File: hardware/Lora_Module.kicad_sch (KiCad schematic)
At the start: 0 parts

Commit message: Main modules added + Com lines
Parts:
- added U7: RFM95W-868S2, RF_Module:HOPERF_RFM9XW_SMD, symbol RF_Module:RFM95W-868S2
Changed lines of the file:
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@@
 	(generator_version "9.0")
 	(paper "A4")
+	(global_label "SPI_SELECT"
+		(shape input)
+		(at 39.37 59.69 180)
+		(fields_autoplaced yes)
+		(effects
+			(font
+				(size 1.27 1.27)
+			)
+			(justify right)
+		)
+		(property "Intersheetrefs" "${INTERSHEET_REFS}"
+			(at 25.5597 59.69 0)
+			(effects
+				(font
+					(size 1.27 1.27)
+				)
+				(justify right)
+				(hide yes)
+			)
+		)
+	)
+	(global_label "SPI_MOSI"
+		(shape input)
+		(at 39.37 62.23 180)
+		(fields_autoplaced yes)
+		(effects
+			(font
+				(size 1.27 1.27)
+			)
+			(justify right)
+		)
+		(property "Intersheetrefs" "${INTERSHEET_REFS}"
+			(at 27.7367 62.23 0)
+			(effects
+				(font
+					(size 1.27 1.27)
+				)
+				(justify right)
+				(hide yes)
+			)
+		)
+	)
+	(global_label "3.3V"
+		(shape input)
+		(at 35.56 38.1 180)
+		(fields_autoplaced yes)
+		(effects
+			(font
+				(size 1.27 1.27)
+			)
+			(justify right)
+		)
+		(property "Intersheetrefs" "${INTERSHEET_REFS}"
+			(at 28.4624 38.1 0)
+			(effects
+				(font
+					(size 1.27 1.27)
+				)
+				(justify right)
+				(hide yes)
+			)
+		)
+	)
+	(global_label "SPI_MISO"
+		(shape output)
+		(at 39.37 64.77 180)
+		(fields_autoplaced yes)
+		(effects
+			(font
+				(size 1.27 1.27)
+			)
+			(justify right)
+		)
+		(property "Intersheetrefs" "${INTERSHEET_REFS}"
+			(at 27.7367 64.77 0)
+			(effects
+				(font
+					(size 1.27 1.27)
+				)
+				(justify right)
+				(hide yes)
+			)
+		)
+	)
+	(global_label "SPI_CLK"
+		(shape input)
+		(at 39.37 67.31 180)
+		(fields_autoplaced yes)
+		(effects
+			(font
+				(size 1.27 1.27)
+			)
+			(justify right)
+		)
+		(property "Intersheetrefs" "${INTERSHEET_REFS}"
+			(at 28.7648 67.31 0)
+			(effects
+				(font
+					(size 1.27 1.27)
+				)
+				(justify right)
+				(hide yes)
+			)
+		)
+	)
+	(symbol
+		(lib_id "RF_Module:RFM95W-868S2")
+		(at 109.22 72.39 0)
+		(unit 1)
+		(exclude_from_sim no)
+		(in_bom yes)
+		(on_board yes)
+		(dnp no)
+		(fields_autoplaced yes)
+		(property "Reference" "U7"
+			(at 111.3633 57.15 0)
+			(effects
+				(font
+					(size 1.27 1.27)
+				)
+				(justify left)
+			)
+		)
+		(property "Value" "RFM95W-868S2"
+			(at 111.3633 59.69 0)
+			(effects
+				(font
+					(size 1.27 1.27)
+				)
+				(justify left)
+			)
+		)
+		(property "Footprint" "RF_Module:HOPERF_RFM9XW_SMD"
+			(at 25.4 30.48 0)
+			(effects
+				(font
+					(size 1.27 1.27)
+				)
+				(hide yes)
+			)
+		)
+		(property "Datasheet" "https://www.hoperf.com/data/upload/portal/20181127/5bfcbea20e9ef.pdf"
+			(at 25.4 30.48 0)
+			(effects
+				(font
+					(size 1.27 1.27)
+				)
+				(hide yes)
+			)
+		)
+		(property "Description" "Low power long range transceiver module, SPI and parallel interface, 868 MHz, spreading factor 6 to12, bandwidth 7.8 to 500kHz, -111 to -148 dBm, SMD-16, DIP-16"
+			(at 109.22 72.39 0)
+			(effects
+				(font
+					(size 1.27 1.27)
+				)
+				(hide yes)
+			)
+		)
+		(pin "3"
+		)
+		(pin "4"
+		)
+		(pin "2"
+		)
+		(pin "5"
+		)
+		(pin "6"
+		)
+		(pin "1"
+		)
+		(pin "13"
+		)
+		(pin "8"
+		)
+		(pin "10"
+		)
+		(pin "9"
+		)
+		(pin "11"
+		)
+		(pin "7"
+		)
+		(pin "14"
+		)
+		(pin "12"
+		)
+		(pin "16"
+		)
+		(pin "15"
+		)
+		(instances
+			(project ""
+				(path "/5b969f6e-a36e-432b-8f00-b2d6a515a877/9db73a32-37a4-4249-8656-c1ba9b3afe01"
+					(reference "U7")
+					(unit 1)
+				)
+			)
+		)
+	)
 )

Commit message: GPS schematic + datasheet
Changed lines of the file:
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@@
 	(global_label "SPI_SELECT"
 		(shape input)
-		(at 39.37 59.69 180)
+		(at 66.04 64.77 180)
 		(fields_autoplaced yes)
 		(effects
@@
 		)
 		(property "Intersheetrefs" "${INTERSHEET_REFS}"
-			(at 25.5597 59.69 0)
+			(at 52.2297 64.77 0)
 			(effects
 				(font
@@
 	(global_label "SPI_MOSI"
 		(shape input)
-		(at 39.37 62.23 180)
+		(at 66.04 67.31 180)
 		(fields_autoplaced yes)
 		(effects
@@
 		)
 		(property "Intersheetrefs" "${INTERSHEET_REFS}"
-			(at 27.7367 62.23 0)
+			(at 54.4067 67.31 0)
 			(effects
 				(font
@@
 	(global_label "3.3V"
 		(shape input)
-		(at 35.56 38.1 180)
+		(at 72.39 53.34 180)
 		(fields_autoplaced yes)
 		(effects
@@
 		)
 		(property "Intersheetrefs" "${INTERSHEET_REFS}"
-			(at 28.4624 38.1 0)
+			(at 65.2924 53.34 0)
 			(effects
 				(font
@@
 	(global_label "SPI_MISO"
 		(shape output)
-		(at 39.37 64.77 180)
+		(at 66.04 69.85 180)
 		(fields_autoplaced yes)
 		(effects
@@
 		)
 		(property "Intersheetrefs" "${INTERSHEET_REFS}"
-			(at 27.7367 64.77 0)
+			(at 54.4067 69.85 0)
 			(effects
 				(font
@@
 	(global_label "SPI_CLK"
 		(shape input)
-		(at 39.37 67.31 180)
+		(at 66.04 72.39 180)
 		(fields_autoplaced yes)
 		(effects
@@
 		)
 		(property "Intersheetrefs" "${INTERSHEET_REFS}"
-			(at 28.7648 67.31 0)
+			(at 55.4348 72.39 0)
 			(effects
 				(font

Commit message: Found all diodes & transistors footprint & JLCPCB
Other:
- company: (none) -> ECAM Brussels Engineering School
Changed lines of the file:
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@@
 	(generator_version "9.0")
 	(paper "A4")
+	(title_block
+		(rev "0.1")
+		(company "ECAM Brussels Engineering School")
+	)
 	(global_label "SPI_SELECT"
 		(shape input)

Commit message: Module Lora
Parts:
- added C10: 100nF, Capacitor_SMD:C_0201_0603Metric, symbol Device:C
- added C11, C12: C, Capacitor_SMD:C_0805_2012Metric_Pad1.18x1.45mm_HandSolder, symbol Device:C
- added J2: 85201239, SMA-85201239:HUBER_SUHNER_85201239, symbol SMA-85201239:85201239
- added R8: 0, Resistor_SMD:R_0805_2012Metric_Pad1.20x1.40mm_HandSolder, symbol Device:R
- added TP_DIO0, TP_RESET, TP_VCC_Lora: TestPoint, TestPoint:TestPoint_Pad_D2.0mm, symbol Connector:TestPoint
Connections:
- net 3.3V: now also U7.13 (3.3V), C10.2, TP_VCC_Lora.1
- net SPI_CLK: now also U7.4 (SCK)
- net SPI_MISO: now also U7.2 (MISO)
- net SPI_MOSI: now also U7.3 (MOSI)
- net SPI_SELECT: now also U7.5 (NSS)
- net GND: now reaches U7.1 (GND)
- net GND: now also U7.10 (GND), U7.8 (GND), C10.1, C11.2, C12.2, J2.G1, J2.G2, J2.G3, J2.G4
- net DIO0: now reaches U7.14 (DIO0)
- net DIO0: now also TP_DIO0.1
- net RESET: now reaches U7.6 (RESET)
- net RESET: now also TP_RESET.1
- net at U7.9 (ANT): now also C12.1, R8.2
- new net: C11.1, J2.1, R8.1

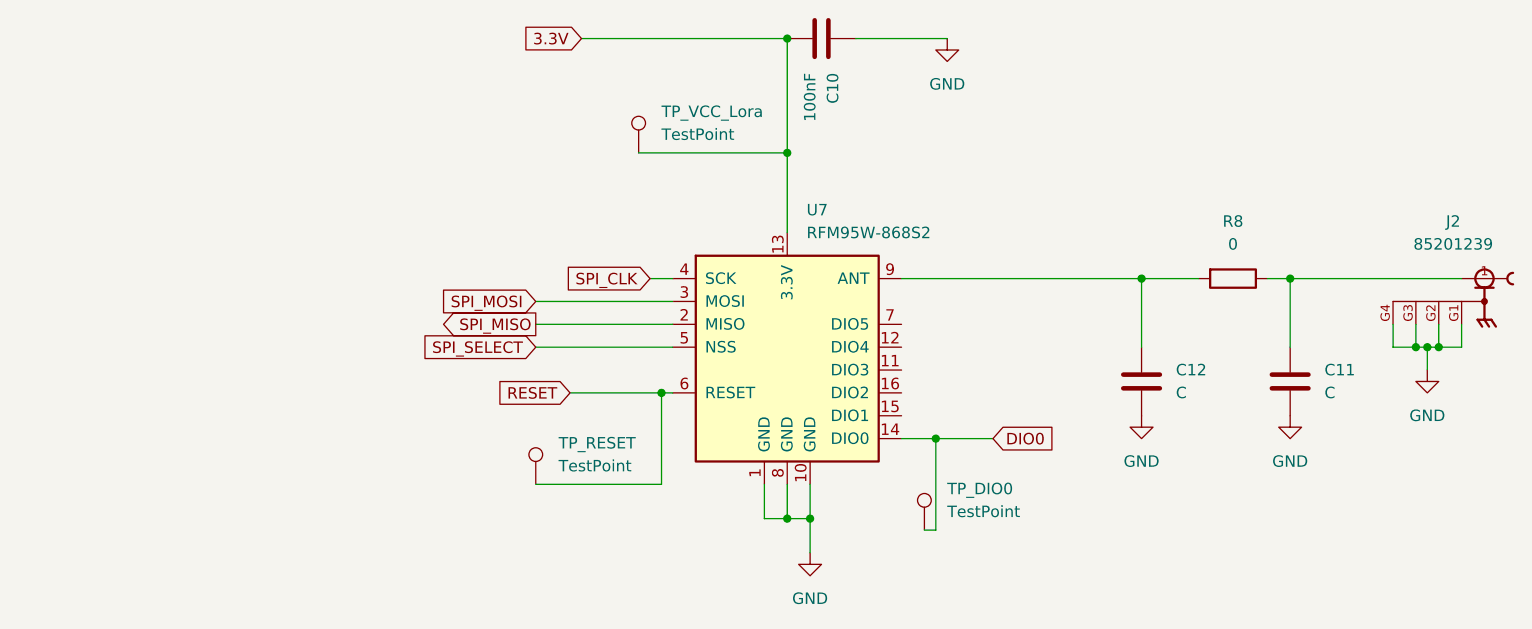
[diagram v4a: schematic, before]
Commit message: Update ESP32 pins
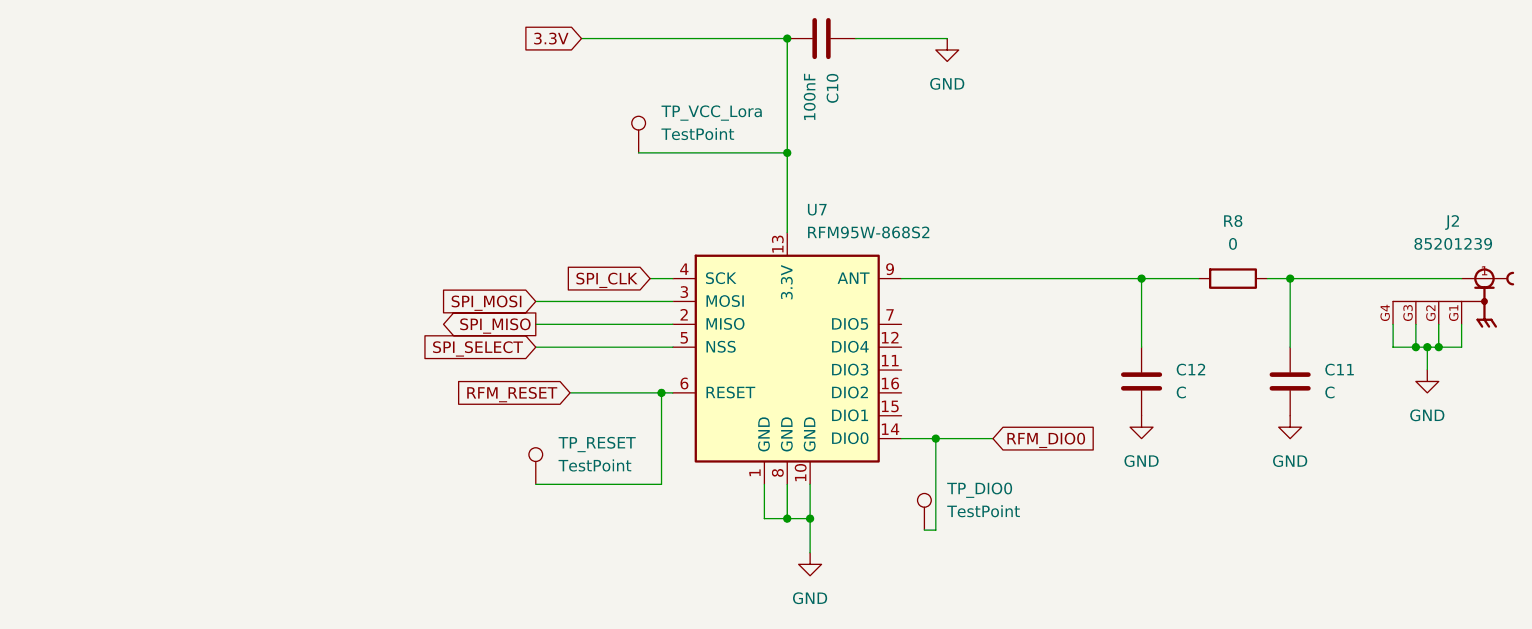
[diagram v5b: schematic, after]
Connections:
- net DIO0 renamed RFM_DIO0
- net RESET renamed RFM_RESET
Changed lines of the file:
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@@
 		)
 	)
-	(global_label "RESET"
+	(global_label "RFM_RESET"
 		(shape input)
 		(at 85.09 77.47 180)
@@
 		)
 		(property "Intersheetrefs" "${INTERSHEET_REFS}"
-			(at 76.3597 77.47 0)
+			(at 71.5821 77.47 0)
 			(effects
 				(font
@@
 		)
 	)
-	(global_label "DIO0"
+	(global_label "RFM_DIO0"
 		(shape input)
 		(at 132.08 82.55 0)
@@
 		)
 		(property "Intersheetrefs" "${INTERSHEET_REFS}"
-			(at 139.48 82.55 0)
+			(at 144.2576 82.55 0)
 			(effects
 				(font

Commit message: First draft
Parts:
- renumbered C10 to C4, C12 to C5, C11 to C6, J2 to J5, R8 to R9, TP_DIO0 to TP_DIO1, TP_RESET to TP_RESET1, TP_VCC_Lora to TP_VCC_Lora1, U7 to U3
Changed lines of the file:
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@@
 		(dnp no)
 		(fields_autoplaced yes)
-		(property "Reference" "TP_DIO0"
+		(property "Reference" "TP_DIO1"
 			(at 127 88.1379 0)
 			(effects
@@
 			(project ""
 				(path "/5b969f6e-a36e-432b-8f00-b2d6a515a877/9db73a32-37a4-4249-8656-c1ba9b3afe01"
-					(reference "TP_DIO0")
+					(reference "TP_DIO1")
 					(unit 1)
 				)
@@
 		(on_board yes)
 		(dnp no)
-		(property "Reference" "J2"
+		(property "Reference" "J5"
 			(at 183.2229 58.42 0)
 			(effects
@@
 			(project ""
 				(path "/5b969f6e-a36e-432b-8f00-b2d6a515a877/9db73a32-37a4-4249-8656-c1ba9b3afe01"
-					(reference "J2")
+					(reference "J5")
 					(unit 1)
 				)
@@
 		(dnp no)
 		(fields_autoplaced yes)
-		(property "Reference" "C12"
+		(property "Reference" "C5"
 			(at 152.4 74.9299 0)
 			(effects
@@
 			(project ""
 				(path "/5b969f6e-a36e-432b-8f00-b2d6a515a877/9db73a32-37a4-4249-8656-c1ba9b3afe01"
-					(reference "C12")
+					(reference "C5")
 					(unit 1)
 				)
@@
 		(dnp no)
 		(fields_autoplaced yes)
-		(property "Reference" "R8"
+		(property "Reference" "R9"
 			(at 158.75 58.42 90)
 			(effects
@@
 			(project ""
 				(path "/5b969f6e-a36e-432b-8f00-b2d6a515a877/9db73a32-37a4-4249-8656-c1ba9b3afe01"
-					(reference "R8")
+					(reference "R9")
 					(unit 1)
 				)
@@
 		(dnp no)
 		(fields_autoplaced yes)
-		(property "Reference" "TP_RESET"
+		(property "Reference" "TP_RESET1"
 			(at 83.82 83.0579 0)
 			(effects
@@
 			(project ""
 				(path "/5b969f6e-a36e-432b-8f00-b2d6a515a877/9db73a32-37a4-4249-8656-c1ba9b3afe01"
-					(reference "TP_RESET")
+					(reference "TP_RESET1")
 					(unit 1)
 				)
@@
 		(dnp no)
 		(fields_autoplaced yes)
-		(property "Reference" "C11"
+		(property "Reference" "C6"
 			(at 168.91 74.9299 0)
 			(effects
@@
 			(project ""
 				(path "/5b969f6e-a36e-432b-8f00-b2d6a515a877/9db73a32-37a4-4249-8656-c1ba9b3afe01"
-					(reference "C11")
+					(reference "C6")
 					(unit 1)
 				)
@@
 		(dnp no)
 		(fields_autoplaced yes)
-		(property "Reference" "U7"
+		(property "Reference" "U3"
 			(at 111.3633 57.15 0)
 			(effects
@@
 			(project ""
 				(path "/5b969f6e-a36e-432b-8f00-b2d6a515a877/9db73a32-37a4-4249-8656-c1ba9b3afe01"
-					(reference "U7")
+					(reference "U3")
 					(unit 1)
 				)
@@
 		(dnp no)
 		(fields_autoplaced yes)
-		(property "Reference" "#PWR06"
+		(property "Reference" "#PWR012"
 			(at 127 44.45 0)
 			(effects
@@
 			(project ""
 				(path "/5b969f6e-a36e-432b-8f00-b2d6a515a877/9db73a32-37a4-4249-8656-c1ba9b3afe01"
-					(reference "#PWR06")
+					(reference "#PWR012")
 					(unit 1)
 				)
@@
 		(dnp no)
 		(fields_autoplaced yes)
-		(property "Reference" "TP_VCC_Lora"
+		(property "Reference" "TP_VCC_Lora1"
 			(at 95.25 46.2279 0)
 			(effects
@@
 			(project ""
 				(path "/5b969f6e-a36e-432b-8f00-b2d6a515a877/9db73a32-37a4-4249-8656-c1ba9b3afe01"
-					(reference "TP_VCC_Lora")
+					(reference "TP_VCC_Lora1")
 					(unit 1)
 				)
@@
 		(dnp no)
 		(fields_autoplaced yes)
-		(property "Reference" "#PWR017"
+		(property "Reference" "#PWR014"
 			(at 165.1 86.36 0)
 			(effects
@@
 			(project ""
 				(path "/5b969f6e-a36e-432b-8f00-b2d6a515a877/9db73a32-37a4-4249-8656-c1ba9b3afe01"
-					(reference "#PWR017")
+					(reference "#PWR014")
 					(unit 1)
 				)
@@
 		(dnp no)
 		(fields_autoplaced yes)
-		(property "Reference" "#PWR018"
+		(property "Reference" "#PWR013"
 			(at 148.59 86.36 0)
 			(effects
@@
 			(project ""
 				(path "/5b969f6e-a36e-432b-8f00-b2d6a515a877/9db73a32-37a4-4249-8656-c1ba9b3afe01"
-					(reference "#PWR018")
+					(reference "#PWR013")
 					(unit 1)
 				)
@@
 		(on_board yes)
 		(dnp no)
-		(property "Reference" "C10"
+		(property "Reference" "C4"
 			(at 114.3001 41.91 0)
 			(effects
@@
 			(project "GOG"
 				(path "/5b969f6e-a36e-432b-8f00-b2d6a515a877/9db73a32-37a4-4249-8656-c1ba9b3afe01"
-					(reference "C10")
+					(reference "C4")
 					(unit 1)
 				)
@@
 		(dnp no)
 		(fields_autoplaced yes)
-		(property "Reference" "#PWR07"
+		(property "Reference" "#PWR011"
 			(at 111.76 101.6 0)
 			(effects
@@
 			(project ""
 				(path "/5b969f6e-a36e-432b-8f00-b2d6a515a877/9db73a32-37a4-4249-8656-c1ba9b3afe01"
-					(reference "#PWR07")
+					(reference "#PWR011")
 					(unit 1)
 				)
@@
 		(dnp no)
 		(fields_autoplaced yes)
-		(property "Reference" "#PWR09"
+		(property "Reference" "#PWR015"
 			(at 180.34 81.28 0)
 			(effects
@@
 			(project ""
 				(path "/5b969f6e-a36e-432b-8f00-b2d6a515a877/9db73a32-37a4-4249-8656-c1ba9b3afe01"
-					(reference "#PWR09")
-					(unit 1)
-				)
+					(reference "#PWR015")
+					(unit 1)
+				)
